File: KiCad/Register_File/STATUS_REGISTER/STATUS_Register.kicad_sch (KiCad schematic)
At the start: 43 parts, among them J1 Conn_01x02_Pin, J10 Conn_01x02_Pin, J11 Conn_01x04_Pin, J2 Conn_01x02_Pin, J3 Conn_01x02_Pin, J5 Conn_01x08_Pin, J6 Conn_01x04_Pin, J7 Conn_01x04_Pin, SW2 SW_SPDT, U1 74LS173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

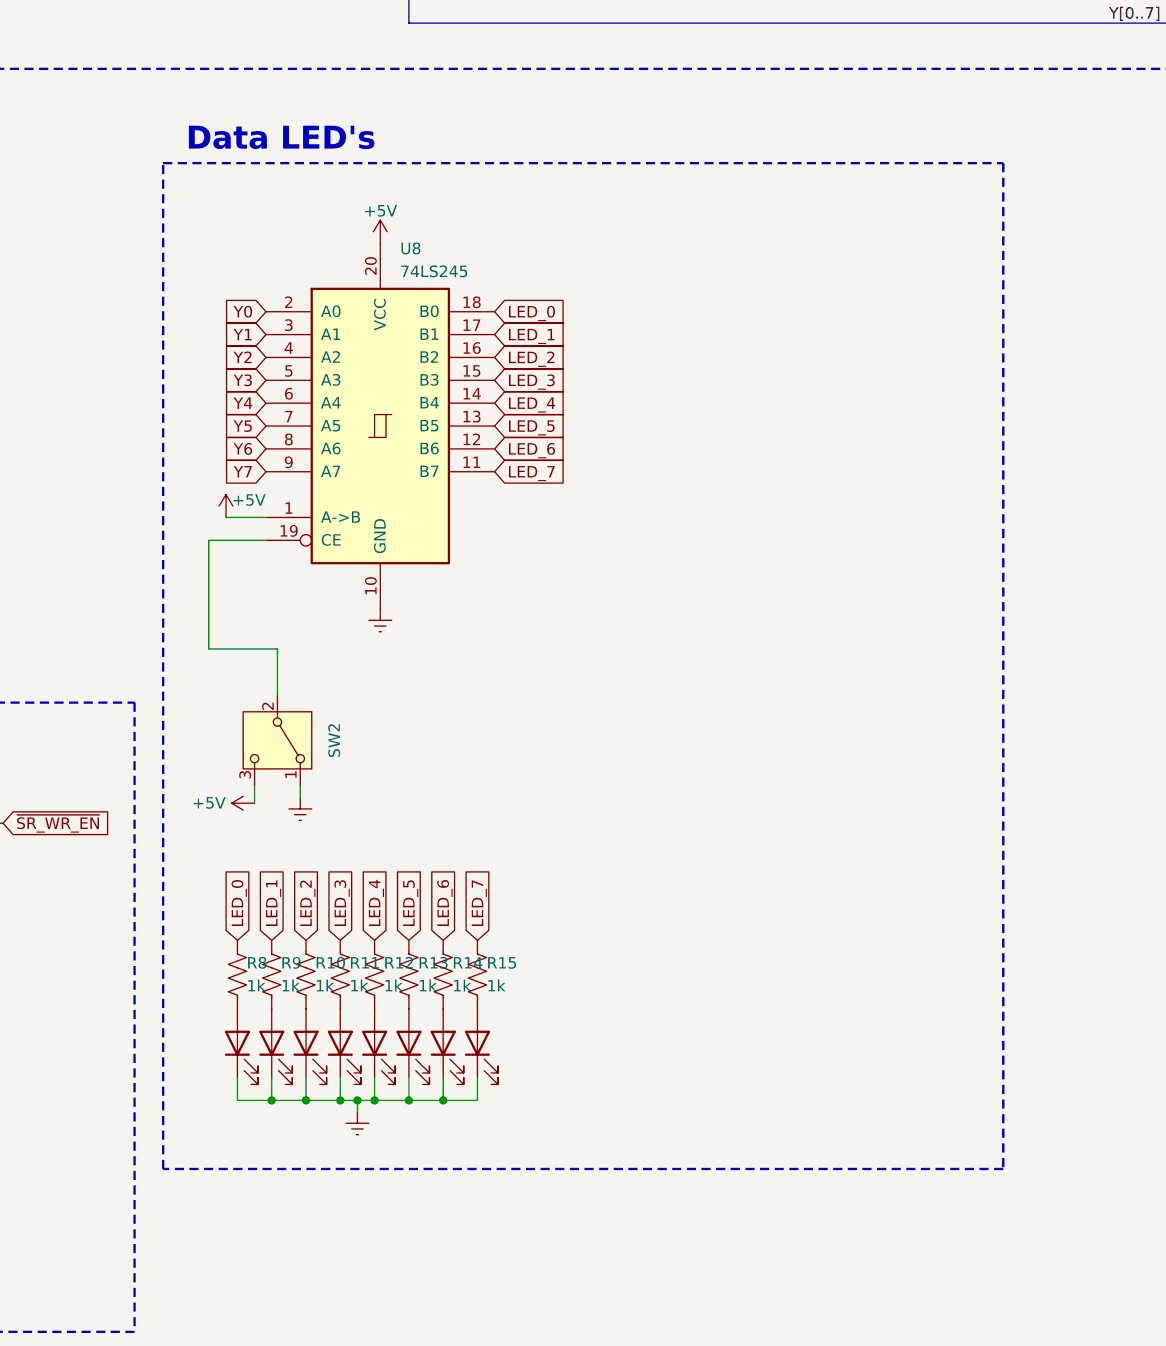
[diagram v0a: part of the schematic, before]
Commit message: added con_ctrl board mdr_mar
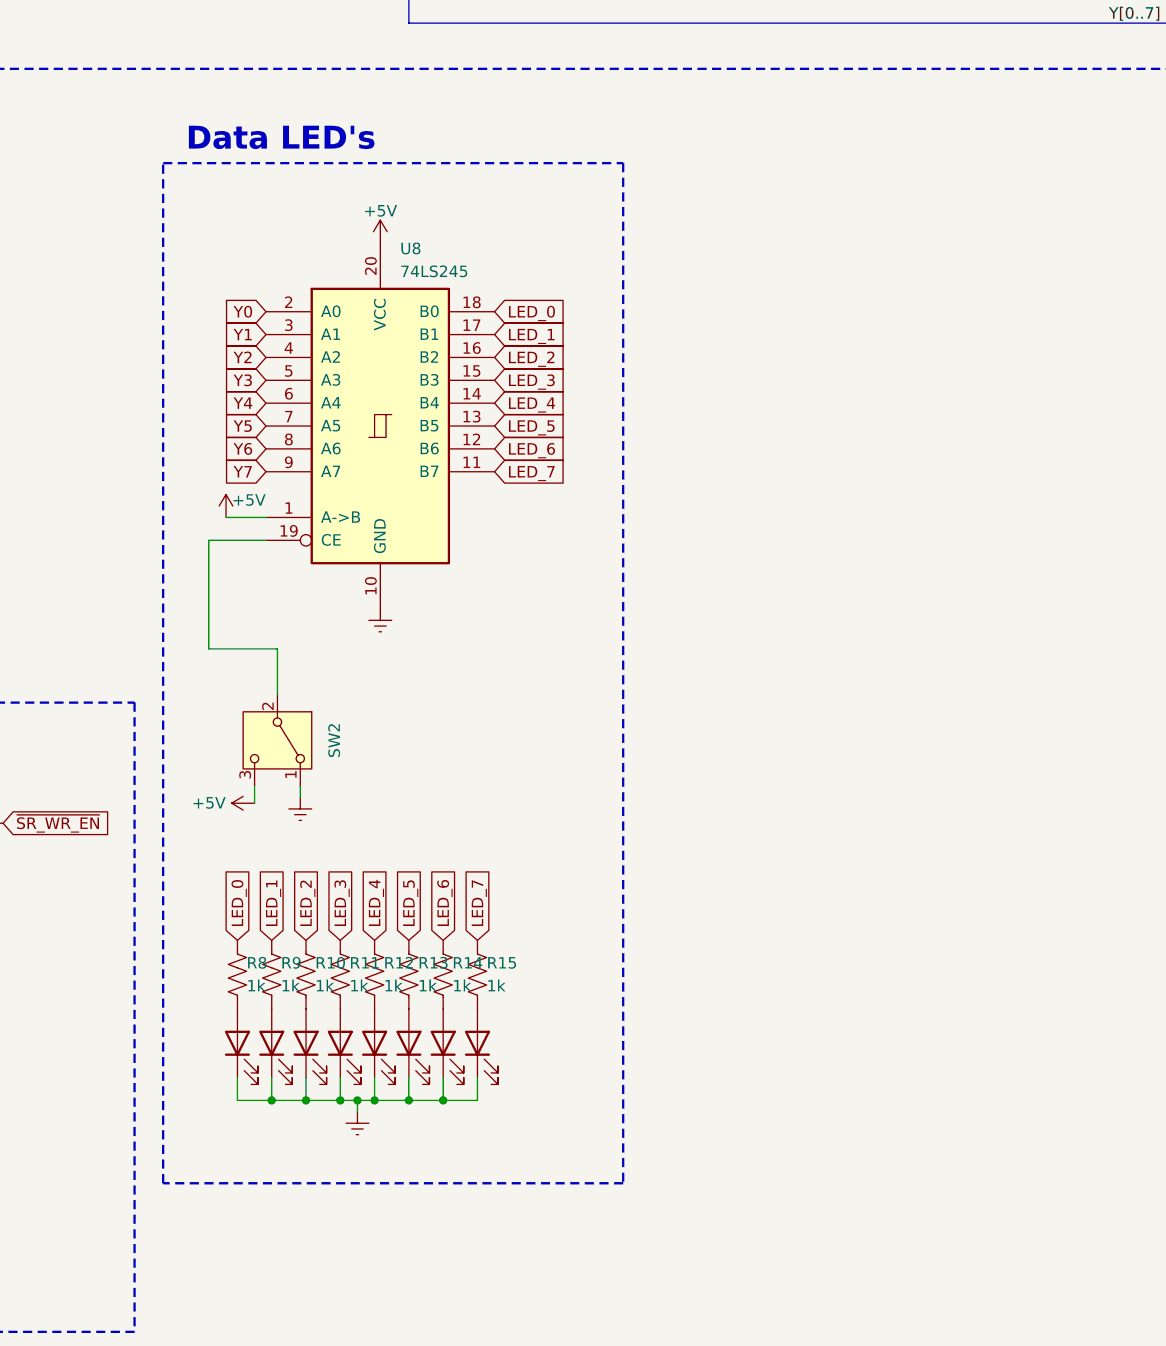
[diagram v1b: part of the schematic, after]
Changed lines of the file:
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@@
 	(rectangle
 		(start 129.8575 110.8075)
-		(end 223.2025 222.5675)
+		(end 180.975 224.155)
 		(stroke
 			(width 0.254)
